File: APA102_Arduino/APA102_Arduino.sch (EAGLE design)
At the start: 16 parts, among them J1 POWER_JACKSMD, U1 V_REG_LD1117, U2 ATMEGA328P-PU

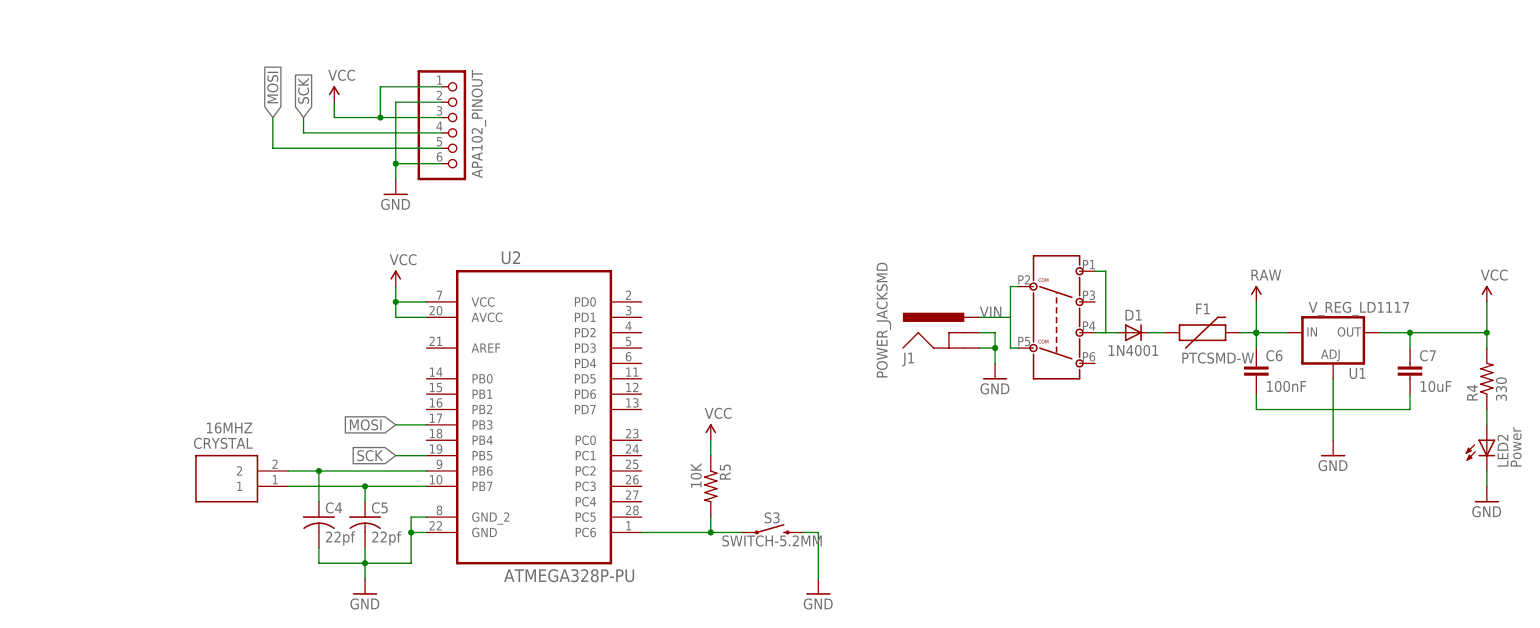
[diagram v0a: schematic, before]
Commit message: Updated design to use the 6-pin header autogenerated from Library.IO that includes a 3D package.
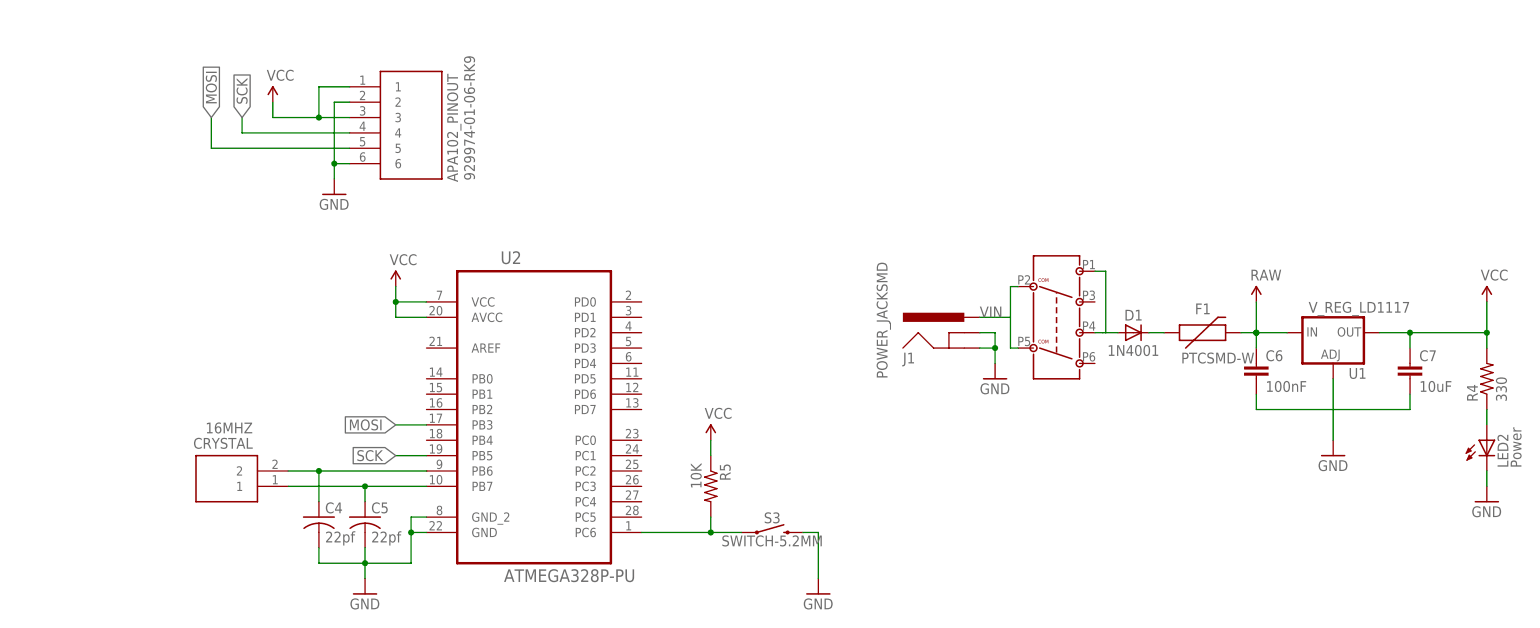
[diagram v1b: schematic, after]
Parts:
- APA102_PINOUT: value (none) -> 929974-01-06-RK9; device pinhead:PINHD-1X6 -> SamacSys_Parts:929974-01-06-RK929974-01-06-RK

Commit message: Updated to include devices containing 3D Objects for crystal and power jack.
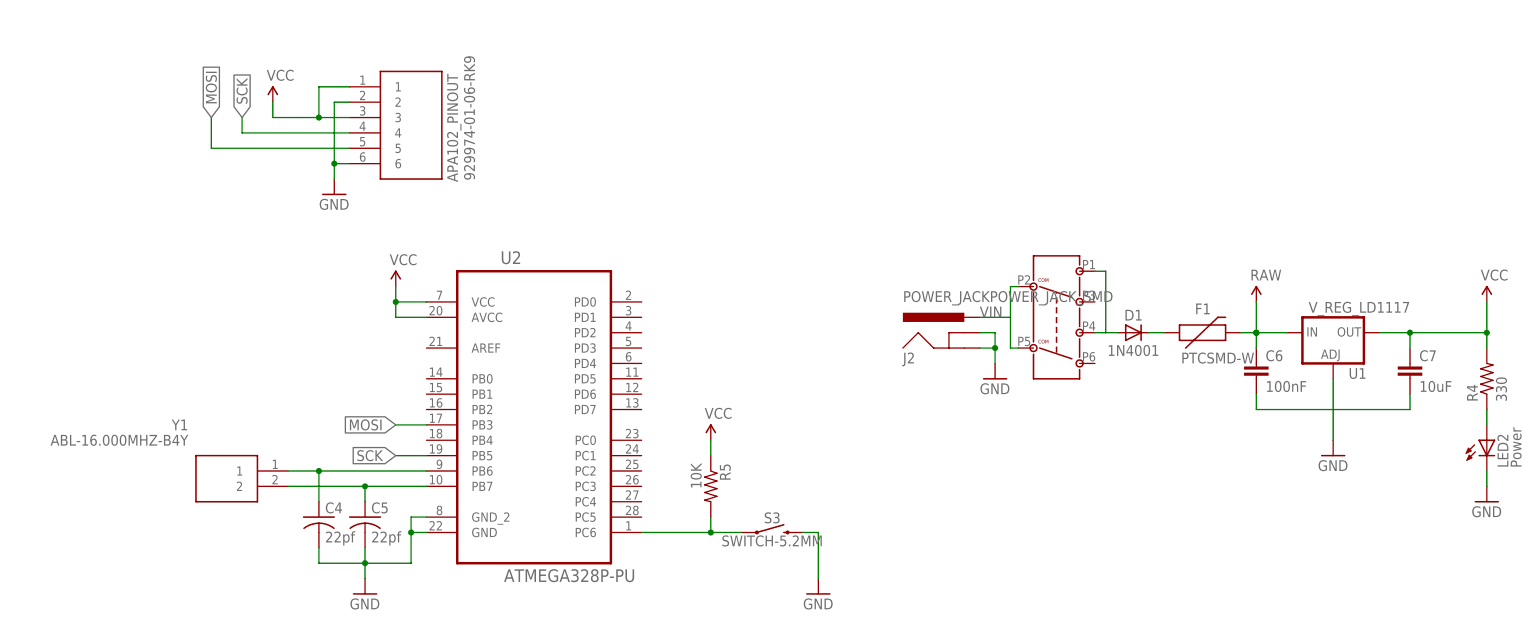
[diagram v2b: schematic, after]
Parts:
- removed CRYSTAL: 16MHZ, SamacSys_Parts:ABL-16.000MHZ-B4Y
- removed J1: POWER_JACKSMD, SparkFun-Connectors:POWER_JACKSMD
- added J2: POWER_JACKPOWER_JACK_SMD, Magister-Libraries:POWER_JACKPOWER_JACK_SMD
- added Y1: ABL-16.000MHZ-B4Y, Magister-Libraries:ABL-16.000MHZ-B4Y
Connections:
- net GND: now also J2.GND, J2.GNDBREAK; no longer J1.GND, J1.GNDBREAK
- net N$3: now also Y1.1; no longer CRYSTAL.2
- net N$6: now also Y1.2; no longer CRYSTAL.1
- net VIN: now also J2.PWR; no longer J1.PWR
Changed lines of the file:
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@@
 <layer number="59" name="tCarbon" color="7" fill="1" visible="no" active="no"/>
 <layer number="60" name="bCarbon" color="7" fill="1" visible="no" active="no"/>
+<layer number="88" name="SimResults" color="9" fill="1" visible="no" active="yes"/>
+<layer number="89" name="SimProbes" color="9" fill="1" visible="no" active="yes"/>
 <layer number="90" name="Modules" color="5" fill="1" visible="yes" active="yes"/>
 <layer number="91" name="Nets" color="2" fill="1" visible="yes" active="yes"/>
@@
 <layer number="113" name="IDFDebug" color="4" fill="1" visible="no" active="no"/>
 <layer number="114" name="CircuitDivider" color="12" fill="0" visible="yes" active="yes"/>
+<layer number="115" name="ReferenceISLANDS" color="7" fill="1" visible="no" active="no"/>
 <layer number="116" name="Patch_BOT" color="9" fill="4" visible="yes" active="yes"/>
+<layer number="117" name="PM_Ref" color="7" fill="1" visible="no" active="no"/>
 <layer number="118" name="Rect_Pads" color="7" fill="1" visible="no" active="no"/>
+<layer number="119" name="PF_Ref" color="7" fill="1" visible="no" active="no"/>
+<layer number="120" name="WFL_Ref" color="7" fill="1" visible="no" active="no"/>
 <layer number="121" name="_tsilk" color="7" fill="1" visible="yes" active="yes"/>
 <layer number="122" name="_bsilk" color="7" fill="1" visible="yes" active="yes"/>
@@
 <part name="RAW" library="SparkFun" deviceset="VCC" device="" value="RAW"/>
 <part name="P+3" library="SparkFun" deviceset="VCC" device=""/>
-<part name="J1" library="SparkFun-Connectors" deviceset="POWER_JACK" device="SMD"/>
 <part name="U2" library="ATMEGA328P-PU" deviceset="ATMEGA328P-PU" device=""/>
 <part name="C4" library="resistor" deviceset="C-US" device="C0805" value="22pf"/>
 <part name="C5" library="resistor" deviceset="C-US" device="C0805" value="22pf"/>
 <part name="GND7" library="SparkFun" deviceset="GND" device=""/>
-<part name="CRYSTAL" library="SamacSys_Parts" deviceset="ABL-16.000MHZ-B4Y" device="" value="16MHZ"/>
 <part name="R5" library="SparkFun" deviceset="RESISTOR" device="0603-RES" value="10K"/>
 <part name="P+1" library="SparkFun" deviceset="VCC" device=""/>
@@
 <part name="C7" library="SparkFun" deviceset="CAP" device="0603-CAP" value="10uF"/>
 <part name="APA102_PINOUT" library="SamacSys_Parts" deviceset="929974-01-06-RK" device="929974-01-06-RK" package3d_urn="urn:adsk.eagle:package:22794030/4" value="929974-01-06-RK9"/>
+<part name="Y1" library="Magister-Libraries" library_urn="urn:adsk.eagle:library:23190065" deviceset="ABL-16.000MHZ-B4Y" device="" package3d_urn="urn:adsk.eagle:package:23090764/3"/>
+<part name="J2" library="Magister-Libraries" library_urn="urn:adsk.eagle:library:23190065" deviceset="POWER_JACK" device="POWER_JACK_SMD" package3d_urn="urn:adsk.eagle:package:23235900/2"/>
 </parts>
 <sheets>
@@
 <attribute name="VALUE" x="214.884" y="56.896" size="1.778" layer="96"/>
 </instance>
-<instance part="J1" gate="G$1" x="129.54" y="43.18" smashed="yes">
-<attribute name="VALUE" x="116.84" y="40.64" size="1.778" layer="96" rot="R90"/>
-<attribute name="NAME" x="119.38" y="43.18" size="1.778" layer="95"/>
-</instance>
 <instance part="U2" gate="A" x="58.42" y="38.1" smashed="yes">
 <attribute name="NAME" x="52.85723125" y="59.6145" size="2.082859375" layer="95" ratio="10" rot="SR0"/>
@@
 <instance part="GND7" gate="1" x="30.48" y="5.08" smashed="yes">
 <attribute name="VALUE" x="27.94" y="2.54" size="1.778" layer="96"/>
-</instance>
-<instance part="CRYSTAL" gate="G$1" x="17.78" y="22.86" smashed="yes" rot="R180">
-<attribute name="NAME" x="11.938" y="29.972" size="1.778" layer="95" rot="R180" align="center-left"/>
-<attribute name="VALUE" x="11.938" y="32.512" size="1.778" layer="96" rot="R180" align="center-left"/>
 </instance>
 <instance part="R5" gate="G$1" x="87.63" y="22.86" smashed="yes" rot="R270">
@@
 <attribute name="NAME" x="44.958" y="73.152" size="1.778" layer="95" rot="R90" align="center-left"/>
 <attribute name="VALUE" x="47.752" y="73.406" size="1.778" layer="96" rot="R90" align="center-left"/>
+</instance>
+<instance part="Y1" gate="G$1" x="17.78" y="25.4" smashed="yes" rot="MR0">
+<attribute name="NAME" x="1.27" y="33.02" size="1.778" layer="95" rot="MR0" align="center-left"/>
+<attribute name="VALUE" x="1.27" y="30.48" size="1.778" layer="96" rot="MR0" align="center-left"/>
+</instance>
+<instance part="J2" gate="G$1" x="129.54" y="43.18" smashed="yes">
+<attribute name="VALUE" x="119.38" y="53.34" size="1.778" layer="96" font="vector"/>
+<attribute name="NAME" x="119.38" y="43.18" size="1.778" layer="95" font="vector"/>
 </instance>
 </instances>
@@
 <junction x="134.62" y="45.72"/>
 <pinref part="GND6" gate="1" pin="GND"/>
-<pinref part="J1" gate="G$1" pin="GND"/>
-<pinref part="J1" gate="G$1" pin="GNDBREAK"/>
+<pinref part="J2" gate="G$1" pin="GNDBREAK"/>
+<pinref part="J2" gate="G$1" pin="GND"/>
 </segment>
 <segment>
@@
 <wire x1="132.08" y1="50.8" x2="137.16" y2="50.8" width="0.1524" layer="91"/>
 <label x="132.08" y="50.8" size="1.778" layer="95"/>
-<pinref part="J1" gate="G$1" pin="PWR"/>
+<pinref part="J2" gate="G$1" pin="PWR"/>
 </segment>
 <segment>
@@
 <pinref part="U2" gate="A" pin="PB6"/>
 <wire x1="40.64" y1="25.4" x2="22.86" y2="25.4" width="0.1524" layer="91"/>
-<pinref part="CRYSTAL" gate="G$1" pin="2"/>
 <pinref part="C4" gate="G$1" pin="1"/>
 <wire x1="22.86" y1="25.4" x2="17.78" y2="25.4" width="0.1524" layer="91"/>
 <wire x1="22.86" y1="20.32" x2="22.86" y2="25.4" width="0.1524" layer="91"/>
 <junction x="22.86" y="25.4"/>
+<pinref part="Y1" gate="G$1" pin="1"/>
 </segment>
 </net>
@@
 <pinref part="U2" gate="A" pin="PB7"/>
 <wire x1="40.64" y1="22.86" x2="30.48" y2="22.86" width="0.1524" layer="91"/>
-<pinref part="CRYSTAL" gate="G$1" pin="1"/>
 <pinref part="C5" gate="G$1" pin="1"/>
 <wire x1="30.48" y1="22.86" x2="17.78" y2="22.86" width="0.1524" layer="91"/>
 <wire x1="30.48" y1="20.32" x2="30.48" y2="22.86" width="0.1524" layer="91"/>
 <junction x="30.48" y="22.86"/>
+<pinref part="Y1" gate="G$1" pin="2"/>
 </segment>
 </net>
@@
 </drawing>
 <compatibility>
+<note version="8.2" severity="warning">
+Since Version 8.2, EAGLE supports online libraries. The ids
+of those online libraries will not be understood (or retained)
+with this version.
+</note>
 <note version="8.3" severity="warning">
 Since Version 8.3, EAGLE supports URNs for individual library
